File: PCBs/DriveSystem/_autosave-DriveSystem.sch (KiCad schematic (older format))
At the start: 41 parts, among them J1 Conn_01x05_Male, J10 Conn_01x04_Female, J11 Conn_01x03_Male, J2 Conn_01x14_Female, J3 Conn_01x04_Female, J4 Conn_01x03_Male, J5 Screw_Terminal_01x02, J6 Screw_Terminal_01x02, J7 Conn_01x04_Male, J8 Conn_01x04_Male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

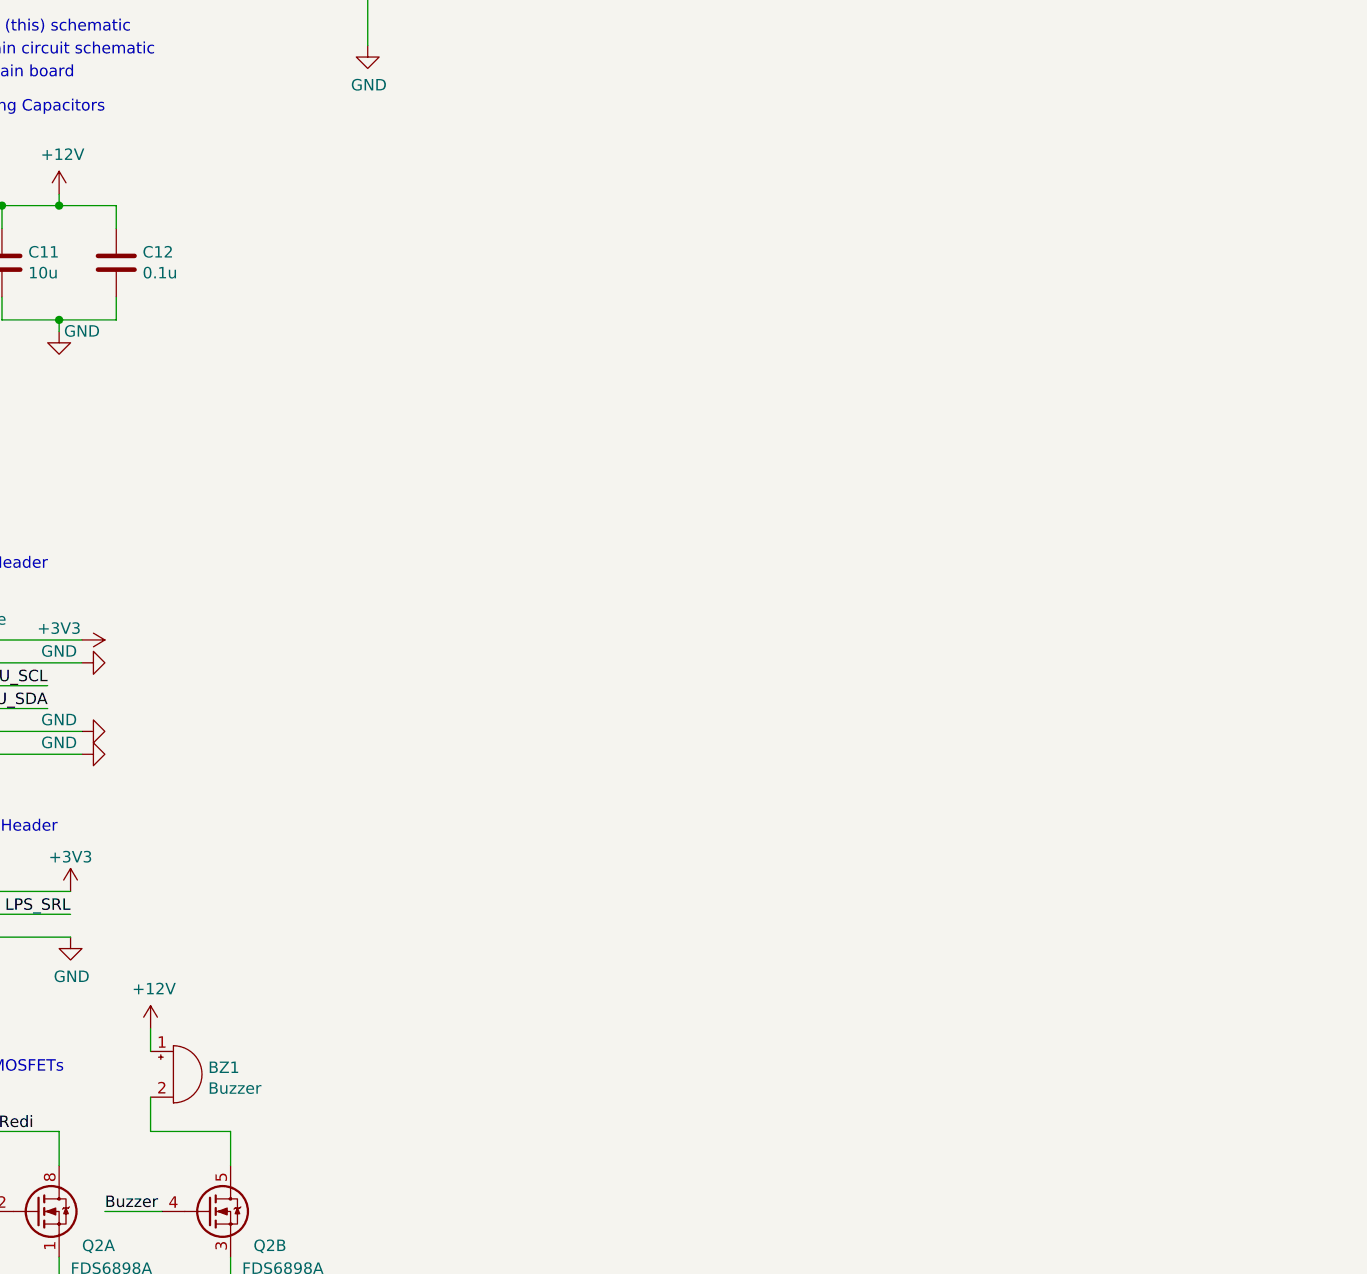
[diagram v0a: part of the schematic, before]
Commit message: added load cell and regulator
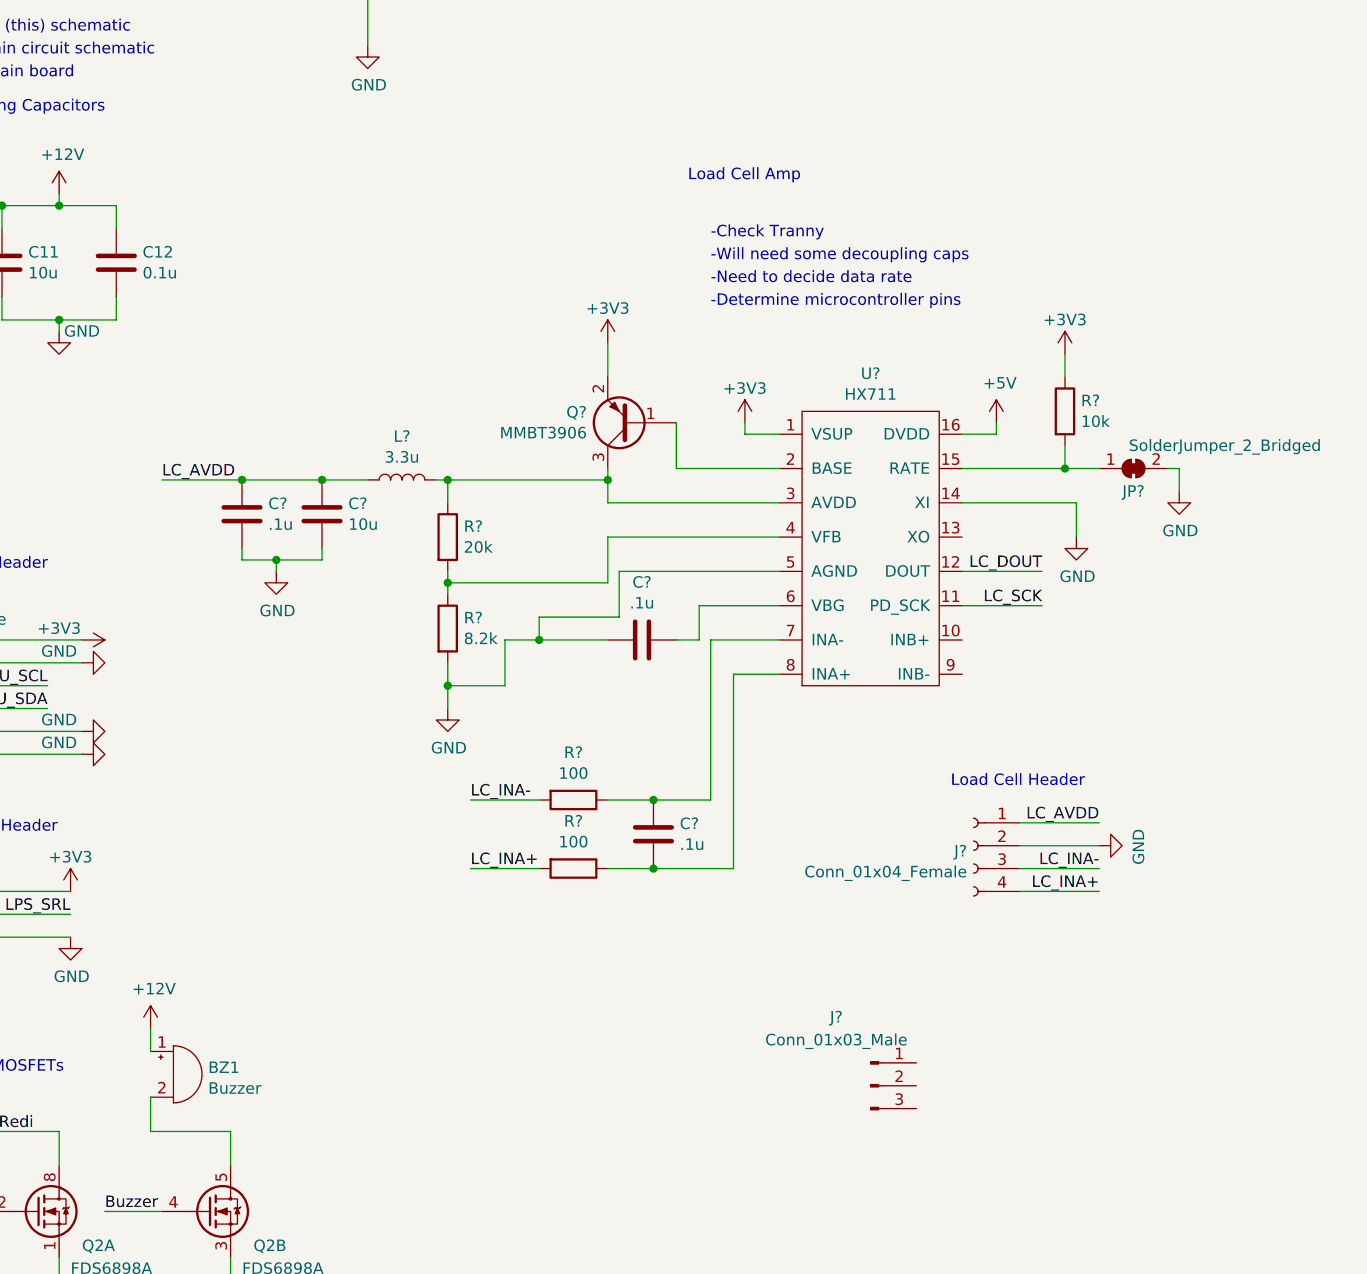
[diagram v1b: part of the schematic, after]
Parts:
- added C? (x3): .1u, symbol Device:C
- added C?: 10u, symbol Device:C
- added J?: Conn_01x04_Female, symbol Connector:Conn_01x04_Female
- added J?: Conn_01x03_Male, Connector_PinHeader_2.54mm:PinHeader_1x01_P2.54mm_Vertical, symbol Connector:Conn_01x03_Male
- added JP?: SolderJumper_2_Bridged, symbol Jumper:SolderJumper_2_Bridged
- added L?: 3.3u, symbol Device:L
- added Q?: MMBT3906, Package_TO_SOT_SMD:SOT-23, symbol Transistor_BJT:MMBT3906
- added R?: 20k, symbol Device:R
- added R?: 8.2k, symbol Device:R
- added R? (x2): 100, symbol Device:R
- added R?: 10k, symbol Device:R
- added U?: HX711, symbol LoadCell:HX711
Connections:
- net +3V3: now also Q?.2 (E), R?.1, U?.1 (VSUP)
- net +5V: now also U?.16 (DVDD)
- net GND: now also C?.1, C?.1, C?.2, J?.2 (Pin_2), JP?.2 (B), R?.2, U?.14 (XI), U?.5 (AGND)
- new net: JP?.1 (A), R?.2, U?.15 (RATE)
- new net: Q?.1 (B), U?.2 (BASE)
- new net: L?.2, Q?.3 (C), R?.1, U?.3 (AVDD)
- new net: R?.1, R?.2, U?.4 (VFB)
- new net: C?.1, U?.6 (VBG)
- new net: C?.2, R?.1, U?.7 (INA-)
- new net: C?.1, R?.1, U?.8 (INA+)
- new net LC_AVDD: C?.2, C?.2, J?.1 (Pin_1), L?.1
- new net LC_DOUT: U?.12 (DOUT)
- new net LC_INA+: J?.4 (Pin_4), R?.2
- new net LC_INA-: J?.3 (Pin_3), R?.2
- new net LC_SCK: U?.11 (PD_SCK)
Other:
- note added: "-Check Tranny\n"
- note added: "-Determine microcontroller pins\n"
- note added: "-Need to decide data rate"
- note added: "-Will need some decoupling caps\n"
- note added: "Load Cell Amp\n"
- note added: "Load Cell Header\n"
